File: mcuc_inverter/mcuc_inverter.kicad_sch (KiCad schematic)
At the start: 0 parts

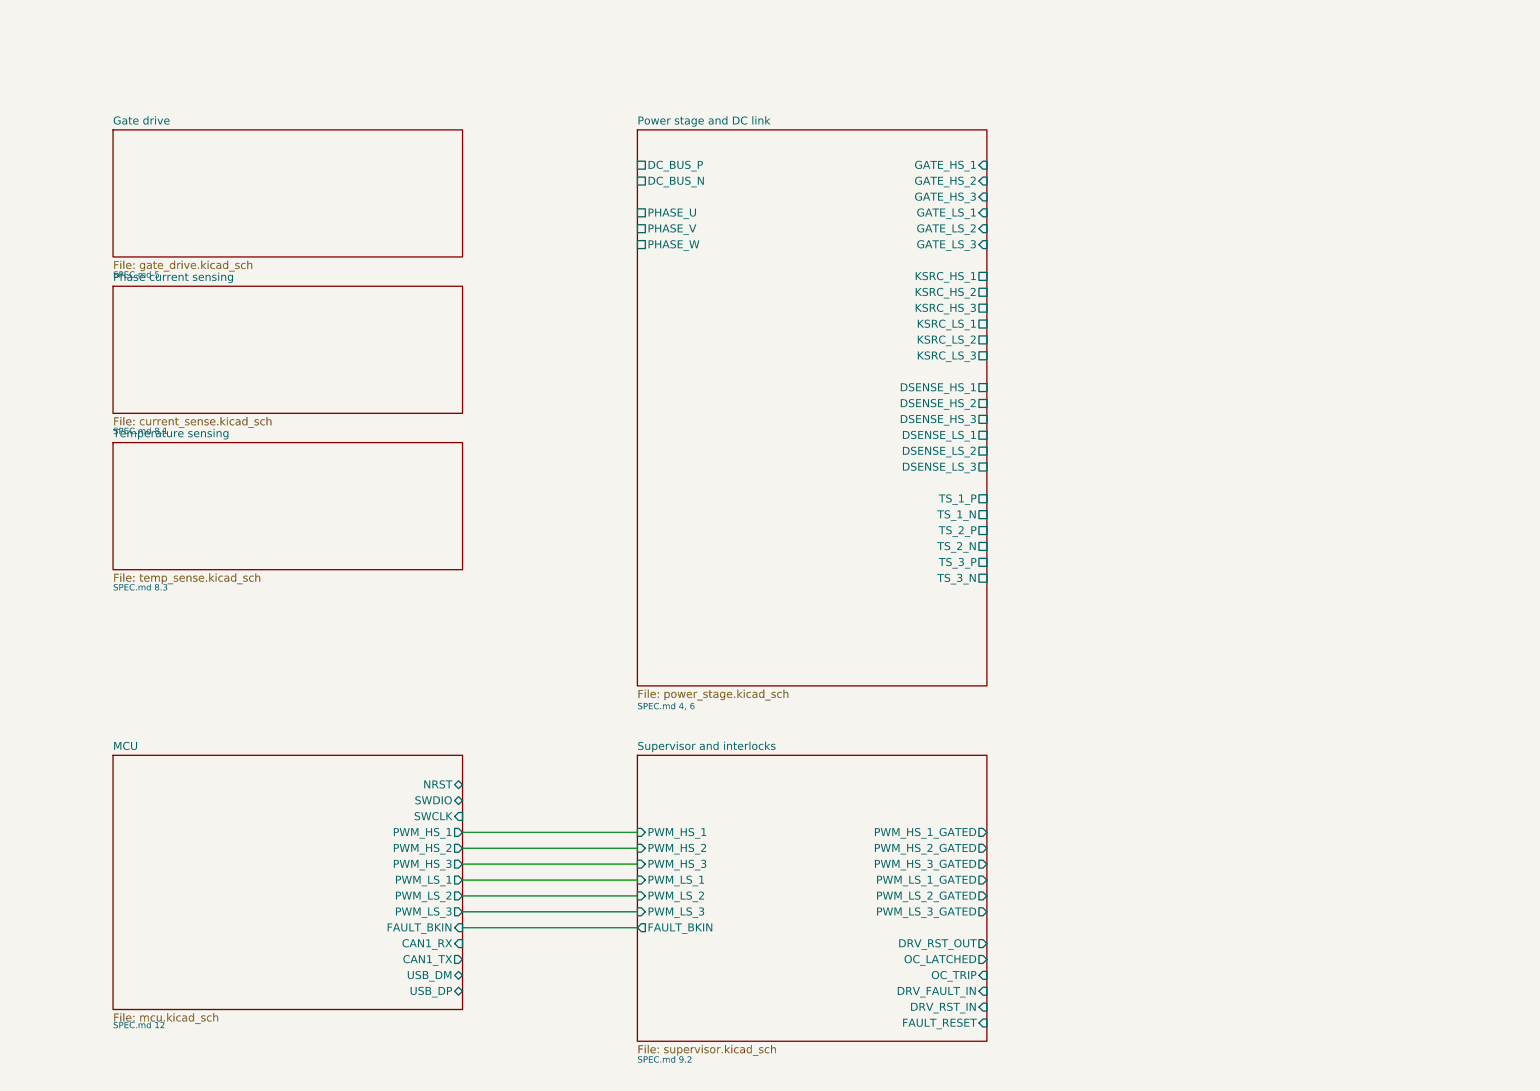
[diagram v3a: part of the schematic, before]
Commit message: Capture gate_drive sheet: 6x 1ED3491MC12M channels, root wiring
Pinout verified from the 1ED34x1Mx12M datasheet v1.20 (single IN pin;
RDYC is dual-function ready-output / fault-clear-input, bused per
datasheet with a 1k series resistor to the supervisor's push-pull
DRV_RST_OUT). Per channel: D018 turn-on RC delay (1k/330p [TBV] with
on-sheet retune note), ON/OFF split gate resistors 12R/3R3, BSS138
Miller clamp to VEE2 per datasheet 4.5.4.1, DESAT chain (1k + 2x
US1M) to the module drain-sense pins, ADJA 4.87k (349 mA soft-off)
and ADJB 1.33k (650 ns LEB) [TBV], +18/-5 rails per HS channel with
shared LS supply. FLT_N wired-AND joins the supervisor fault
conditioning.

Root sheet: supervisor -> gate_drive (gated PWM x6, DRV_FAULT_IN,
DRV_RST_OUT) and gate_drive -> power_stage (GATE/KSRC/DSENSE x6)
wired; VGD_* rails await aux_power.

ERC 0 errors; 244/244 per-channel netlist checks by the capture
agent, key nets independently re-verified before commit.

Co-Authored-By: Claude Fable 5 <noreply@anthropic.com>
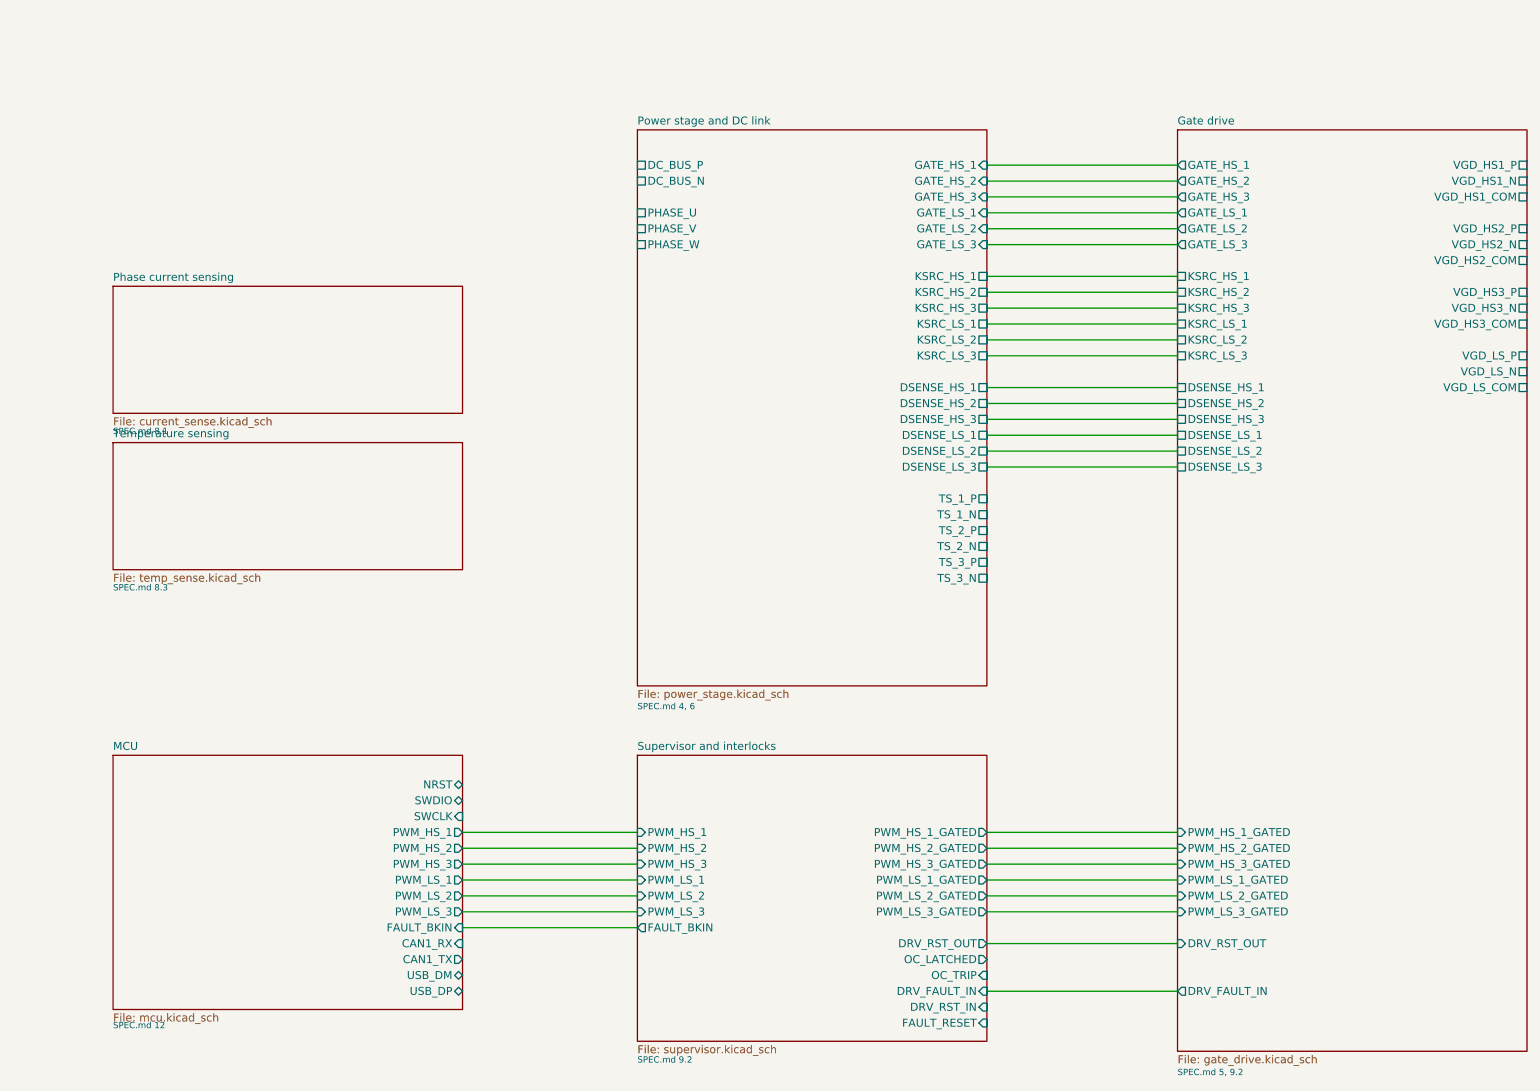
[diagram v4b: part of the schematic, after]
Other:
- sheet Gate drive ports: added DRV_FAULT_IN, DRV_RST_OUT, DSENSE_HS_1, DSENSE_HS_2, DSENSE_HS_3, DSENSE_LS_1, DSENSE_LS_2, DSENSE_LS_3, GATE_HS_1, GATE_HS_2, GATE_HS_3, GATE_LS_1, GATE_LS_2, GATE_LS_3, KSRC_HS_1, KSRC_HS_2, KSRC_HS_3, KSRC_LS_1, KSRC_LS_2, KSRC_LS_3, PWM_HS_1_GATED, PWM_HS_2_GATED, PWM_HS_3_GATED, PWM_LS_1_GATED, PWM_LS_2_GATED, PWM_LS_3_GATED, VGD_HS1_COM, VGD_HS1_N, VGD_HS1_P, VGD_HS2_COM, VGD_HS2_N, VGD_HS2_P, VGD_HS3_COM, VGD_HS3_N, VGD_HS3_P, VGD_LS_COM, VGD_LS_N, VGD_LS_P; removed none
- note added: "SPEC.md 5, 9.2"
- note removed: "SPEC.md 5"

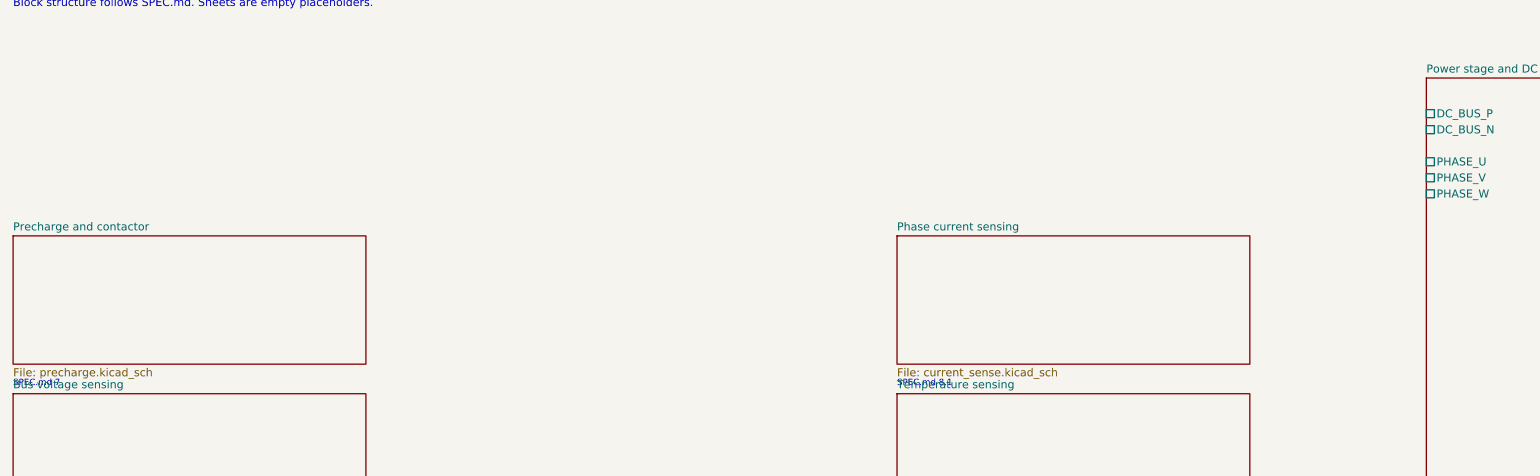
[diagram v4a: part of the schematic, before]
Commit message: Capture precharge sheet: precharge, bleeder, active discharge
Per SPEC 7: precharge path (relay + 1.25k 50W >=41J pulse resistor
into DC_BUS_P), main-contactor low-side driver with flyback diode,
passive bleeder as a strict 4-resistor series string (no part spans
450 V, SPEC 8.2 rule), and active discharge (4x 220R 25W string +
C3M0350120J, opto-driven gate with 18 V zener clamp, floating supply
labels pending aux_power; VDISCH_N tied to the FET source on-sheet).
Sequencing rule and discharge requirements quoted on-sheet.

Root: DC_BUS_P/N wired precharge <-> power_stage; verified in the
netlist that the precharge resistor output reaches the module P1-P3
terminals and cap bank. ERC 0 errors; 40/40 structural netlist
assertions by the capture agent; HV/LV separation independently
re-verified (no HV net shares a pin with GND/+3.3V/+12V).

Co-Authored-By: Claude Fable 5 <noreply@anthropic.com>
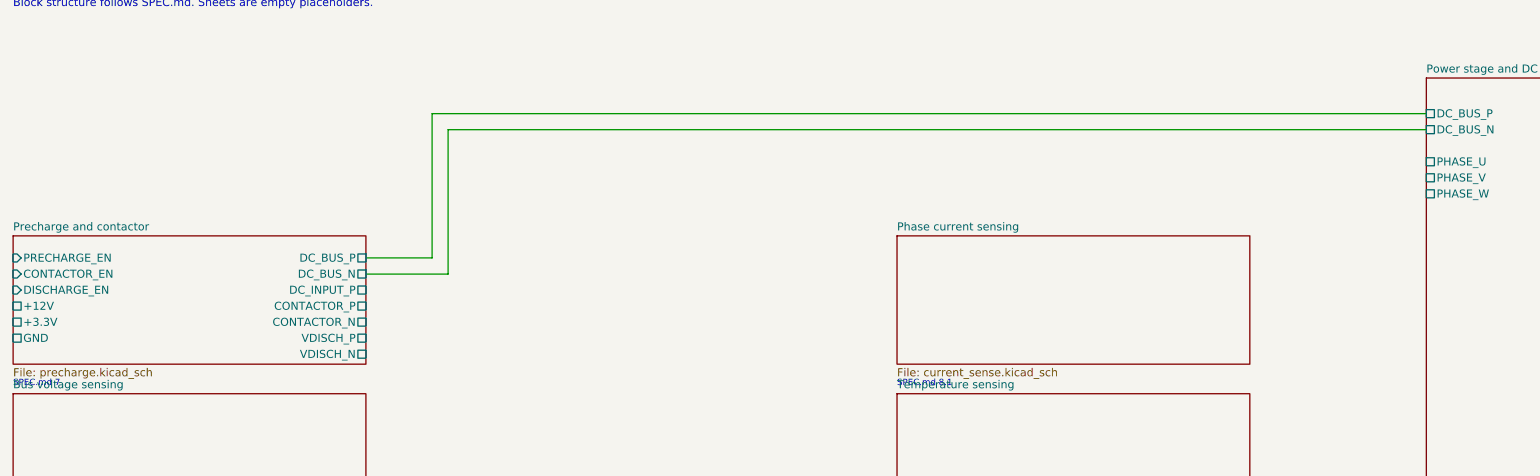
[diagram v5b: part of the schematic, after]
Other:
- sheet Precharge and contactor ports: added +12V, +3.3V, CONTACTOR_EN, CONTACTOR_N, CONTACTOR_P, DC_BUS_N, DC_BUS_P, DC_INPUT_P, DISCHARGE_EN, GND, PRECHARGE_EN, VDISCH_N, VDISCH_P; removed none
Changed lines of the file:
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@@
+			)
+		)
+		(pin "PRECHARGE_EN" input
+			(at 20.0 63.5 180)
+			(effects
+				(font
+					(size 1.27 1.27)
+				)
+				(justify left)
+			)
+		)
+		(pin "CONTACTOR_EN" input
+			(at 20.0 66.04 180)
+			(effects
+				(font
+					(size 1.27 1.27)
+				)
+				(justify left)
+			)
+		)
+		(pin "DISCHARGE_EN" input
+			(at 20.0 68.58 180)
+			(effects
+				(font
+					(size 1.27 1.27)
+				)
+				(justify left)
+			)
+		)
+		(pin "+12V" passive
+			(at 20.0 71.12 180)
+			(effects
+				(font
+					(size 1.27 1.27)
+				)
+				(justify left)
+			)
+		)
+		(pin "+3.3V" passive
+			(at 20.0 73.66 180)
+			(effects
+				(font
+					(size 1.27 1.27)
+				)
+				(justify left)
+			)
+		)
+		(pin "GND" passive
+			(at 20.0 76.2 180)
+			(effects
+				(font
+					(size 1.27 1.27)
+				)
+				(justify left)
+			)
+		)
+		(pin "DC_BUS_P" passive
+			(at 75.88 63.5 0)
+			(effects
+				(font
+					(size 1.27 1.27)
+				)
+				(justify right)
+			)
+		)
+		(pin "DC_BUS_N" passive
+			(at 75.88 66.04 0)
+			(effects
+				(font
+					(size 1.27 1.27)
+				)
+				(justify right)
+			)
+		)
+		(pin "DC_INPUT_P" passive
+			(at 75.88 68.58 0)
+			(effects
+				(font
+					(size 1.27 1.27)
+				)
+				(justify right)
+			)
+		)
+		(pin "CONTACTOR_P" passive
+			(at 75.88 71.12 0)
+			(effects
+				(font
+					(size 1.27 1.27)
+				)
+				(justify right)
+			)
+		)
+		(pin "CONTACTOR_N" passive
+			(at 75.88 73.66 0)
+			(effects
+				(font
+					(size 1.27 1.27)
+				)
+				(justify right)
+			)
+		)
+		(pin "VDISCH_P" passive
+			(at 75.88 76.2 0)
+			(effects
+				(font
+					(size 1.27 1.27)
+				)
+				(justify right)
+			)
+		)
+		(pin "VDISCH_N" passive
+			(at 75.88 78.74 0)
+			(effects
+				(font
+					(size 1.27 1.27)
+				)
+				(justify right)
 			)
 		)
@@
 		)
 		(stroke
+			(width 0)
+			(type default)
+		)
+	)
+	(wire
+		(pts
+			(xy 75.88 63.5) (xy 86.36 63.5)
+		)
+		(stroke
+			(width 0)
+			(type default)
+		)
+	)
+	(wire
+		(pts
+			(xy 86.36 40.64) (xy 86.36 63.5)
+		)
+		(stroke
+			(width 0)
+			(type default)
+		)
+	)
+	(wire
+		(pts
+			(xy 86.36 40.64) (xy 243.84 40.64)
+		)
+		(stroke
+			(width 0)
+			(type default)
+		)
+	)
+	(wire
+		(pts
+			(xy 75.88 66.04) (xy 88.9 66.04)
+		)
+		(stroke
+			(width 0)
+			(type default)
+		)
+	)
+	(wire
+		(pts
+			(xy 88.9 43.18) (xy 88.9 66.04)
+		)
+		(stroke
+			(width 0)
+			(type default)
+		)
+	)
+	(wire
+		(pts
+			(xy 88.9 43.18) (xy 243.84 43.18)
+		)
+		(stroke
